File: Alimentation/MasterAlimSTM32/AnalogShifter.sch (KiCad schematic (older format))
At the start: 4 parts

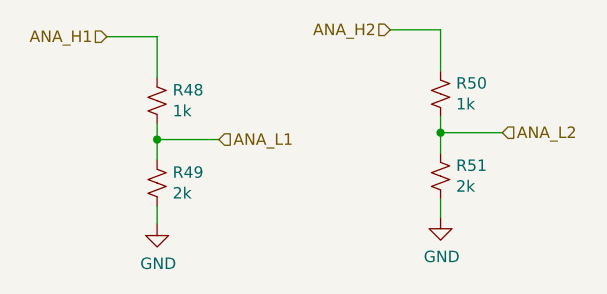
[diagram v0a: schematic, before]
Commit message: Module alim ISO, clean master alim
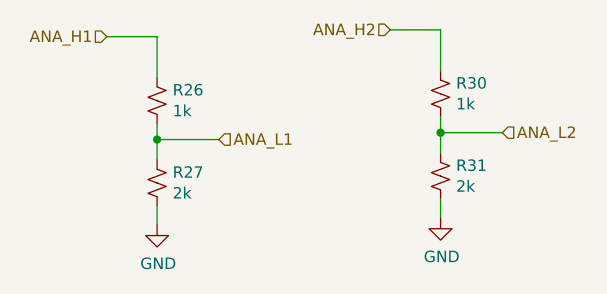
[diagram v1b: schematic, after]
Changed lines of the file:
@@
 AR Path="/60C868EA/60B781F4" Ref="R44"  Part="1"
 AR Path="/60C872D4/60B781F4" Ref="R48"  Part="1"
-F 0 "R48" H 4858 2996 50  0000 L CNN
+F 0 "R26" H 4858 2996 50  0000 L CNN
 F 1 "1k" H 4858 2905 50  0000 L CNN
 F 2 "" H 4790 2950 50  0001 C CNN
@@
 AR Path="/60C868EA/60B78705" Ref="R45"  Part="1"
 AR Path="/60C872D4/60B78705" Ref="R49"  Part="1"
-F 0 "R49" H 4858 3356 50  0000 L CNN
+F 0 "R27" H 4858 3356 50  0000 L CNN
 F 1 "2k" H 4858 3265 50  0000 L CNN
 F 2 "" H 4790 3310 50  0001 C CNN
@@
 AR Path="/60C868EA/60B78AB4" Ref="#PWR0169"  Part="1"
 AR Path="/60C872D4/60B78AB4" Ref="#PWR0171"  Part="1"
-F 0 "#PWR0171" H 4790 3240 50  0001 C CNN
+F 0 "#PWR0161" H 4790 3240 50  0001 C CNN
 F 1 "GND" H 4795 3317 50  0000 C CNN
 F 2 "" H 4790 3490 50  0001 C CNN
@@
 AR Path="/60C868EA/60B7A51D" Ref="R46"  Part="1"
 AR Path="/60C872D4/60B7A51D" Ref="R50"  Part="1"
-F 0 "R50" H 6098 2966 50  0000 L CNN
+F 0 "R30" H 6098 2966 50  0000 L CNN
 F 1 "1k" H 6098 2875 50  0000 L CNN
 F 2 "" H 6030 2920 50  0001 C CNN
@@
 AR Path="/60C868EA/60B7A565" Ref="R47"  Part="1"
 AR Path="/60C872D4/60B7A565" Ref="R51"  Part="1"
-F 0 "R51" H 6098 3326 50  0000 L CNN
+F 0 "R31" H 6098 3326 50  0000 L CNN
 F 1 "2k" H 6098 3235 50  0000 L CNN
 F 2 "" H 6030 3280 50  0001 C CNN
@@
 AR Path="/60C868EA/60B7A56F" Ref="#PWR0170"  Part="1"
 AR Path="/60C872D4/60B7A56F" Ref="#PWR0172"  Part="1"
-F 0 "#PWR0172" H 6030 3210 50  0001 C CNN
+F 0 "#PWR0162" H 6030 3210 50  0001 C CNN
 F 1 "GND" H 6035 3287 50  0000 C CNN
 F 2 "" H 6030 3460 50  0001 C CNN
